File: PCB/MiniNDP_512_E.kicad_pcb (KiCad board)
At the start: 2 copper layers, 60 x 34 mm, 26 parts, among them J1 Conn_02x20_Odd_Even, U1 HC161, U2 HC161, U3 HC161, U4 HC138, U5 74xx574, U6 AS6C4008, U7 1G32, U8 1G79

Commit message: E board
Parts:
- U5: value 74xx574 -> HC574

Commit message: E board
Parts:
- moved C2 0.65 mm to (158.7, 90.5)

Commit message: E board
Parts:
- moved C2 0.05 mm to (158.7, 90.5)
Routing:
- net GND: vias 60 -> 61

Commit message: E board
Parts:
- removed the C4 at (131.8, 99.9)
- removed C6: 1u, 000_LOCAL:C_0805
- moved JP1 3.09 mm to (147.7, 109.0), turned to 180 degrees
- moved U8 3.01 mm to (147.7, 108.0), turned to -90 degrees
- moved C4 2.60 mm to (131.7, 92.3), turned to 90 degrees
- moved C5 2.19 mm to (139.7, 99.7), turned to 180 degrees
- moved U5 0.75 mm to (138.1, 104.3)
- renumbered C5 to C4, C7 to C5
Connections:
- U4 pad 1: /BUS_A8 -> GND
- U4 pad 11: unconnected-(U4-O4-Pad11) -> /~{BLOCK}
- U4 pad 12: /~{BYTE} -> unconnected-(U4-O3-Pad12)
- U4 pad 14: /~{BLOCK} -> unconnected-(U4-O1-Pad14)
- U4 pad 3: GND -> /BUS_A8
- U4 pad 4: GND -> /~{Y0}
- U4 pad 5: /~{Y0} -> GND
- U4 pad 9: unconnected-(U4-O6-Pad9) -> /~{BYTE}
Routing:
- net VBUS: track 121.7 -> 93.7 mm, vias 11 -> 8
- net /~{BYTE}: track 53.9 -> 50.3 mm, vias 6 -> 4
- net /BUS_A8: track 17.5 -> 19.8 mm
- net /~{BLOCK}: track 52.3 -> 50.0 mm, vias 2 -> 5
- net /A18: track 21.3 -> 23.0 mm
- net /BUS_A10: track 11.9 -> 10.3 mm
- net /~{RD}: track 36.3 -> 34.8 mm
- net /A11: track 22.3 -> 21.3 mm
- net /A10: track 22.1 -> 21.2 mm
- net /A12: track 21.5 -> 20.9 mm
- net GND: vias 61 -> 41

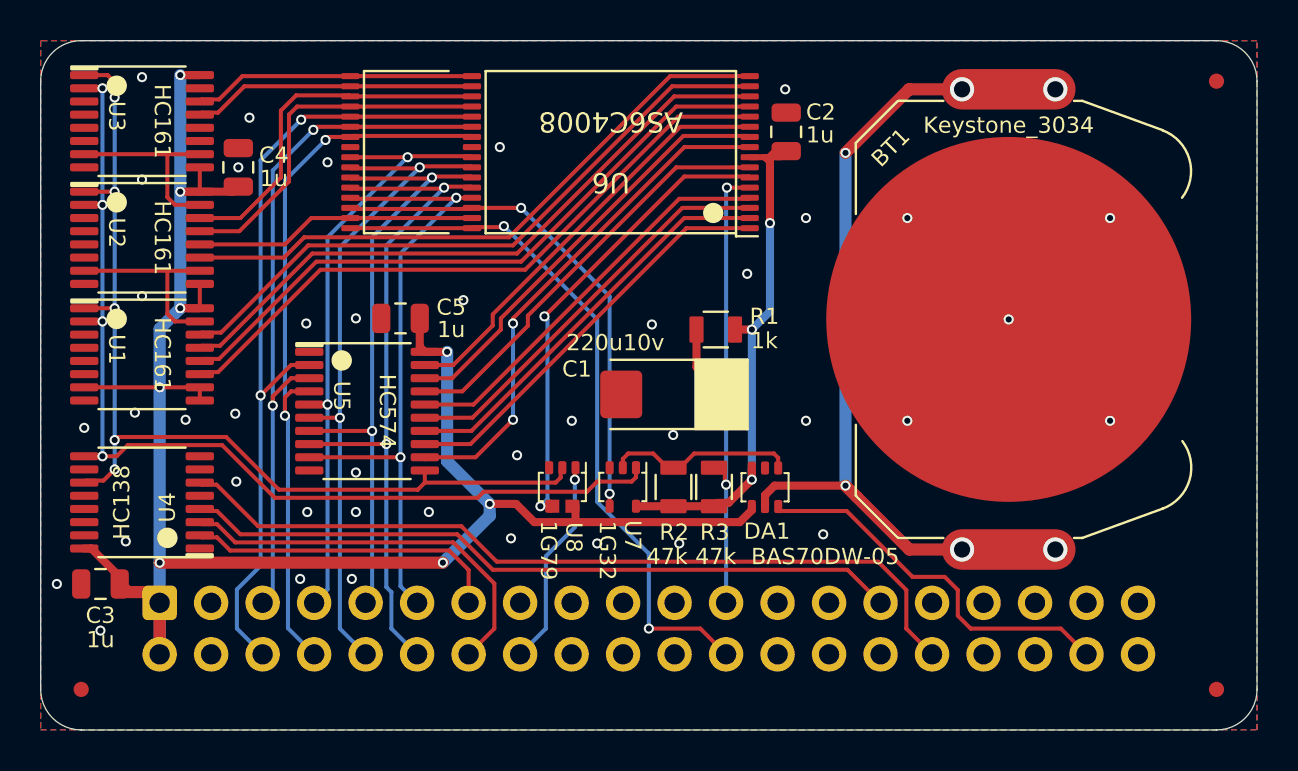
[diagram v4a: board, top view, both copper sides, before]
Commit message: E02 position HC574
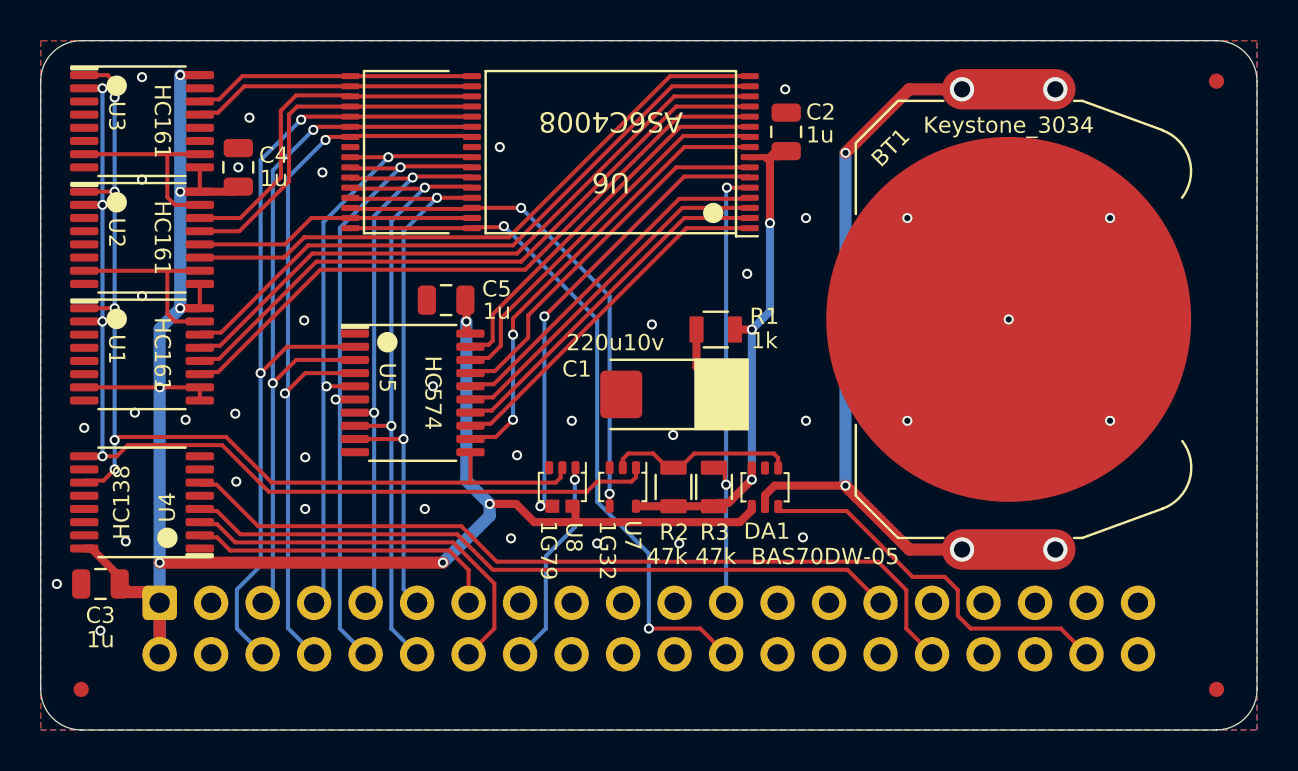
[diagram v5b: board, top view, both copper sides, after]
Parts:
- moved C5 2.42 mm to (142.0, 98.8)
- moved U5 2.42 mm to (140.3, 103.4)
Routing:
- net /A17: track 25.4 -> 22.7 mm
- net /A14: track 20.3 -> 17.7 mm
- net /A15: track 20.4 -> 17.8 mm
- net /A16: track 20.4 -> 17.8 mm
- net /A13: track 20.2 -> 17.6 mm
- net /AD7: track 32.0 -> 29.4 mm
- net /AD6: track 34.7 -> 32.1 mm
- net /AD5: track 31.5 -> 29.0 mm
- net /A12: track 20.9 -> 18.6 mm
- net /A10: track 21.2 -> 19.0 mm
- net /AD0: track 39.7 -> 41.9 mm
- net /A11: track 21.3 -> 19.2 mm
- net /AD1: track 34.9 -> 36.8 mm
- net /AD2: track 36.3 -> 38.0 mm
- net /AD4: track 33.8 -> 33.0 mm
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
